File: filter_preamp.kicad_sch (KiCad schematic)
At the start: 24 parts, among them J2 Conn_Coaxial, Q1 2N2222A, Q2 2N2222A

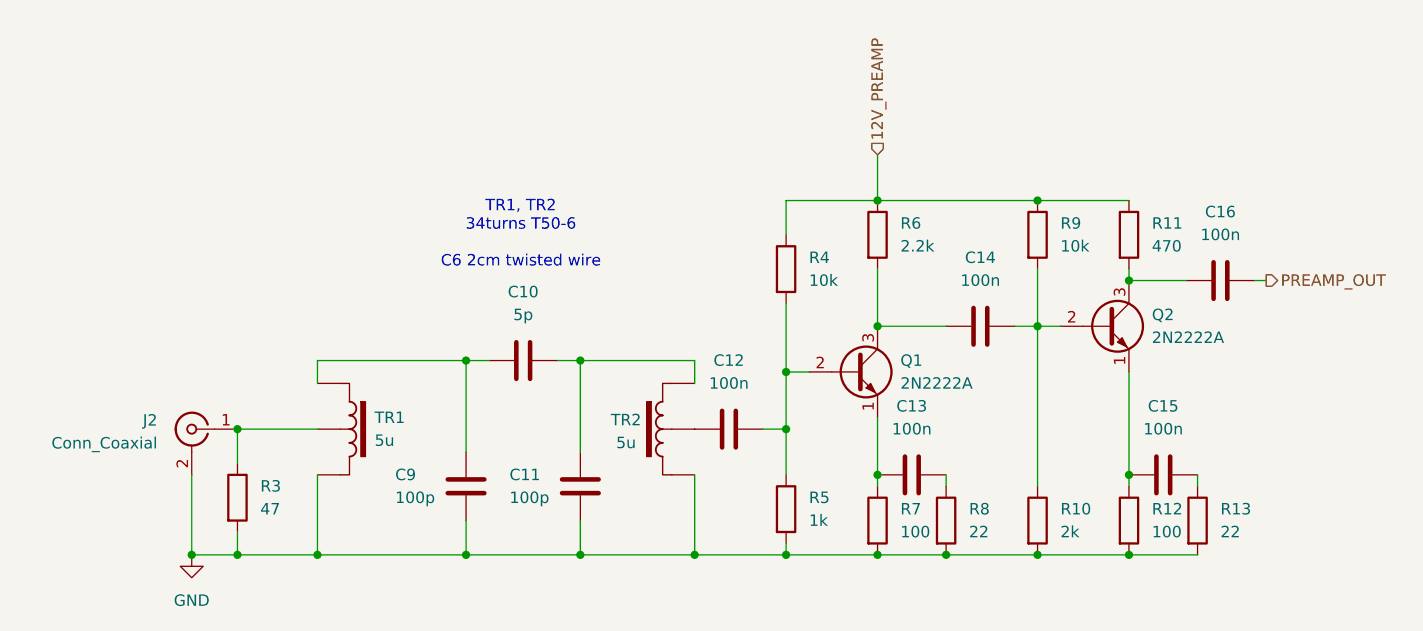
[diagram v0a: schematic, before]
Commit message: Update transformer comment
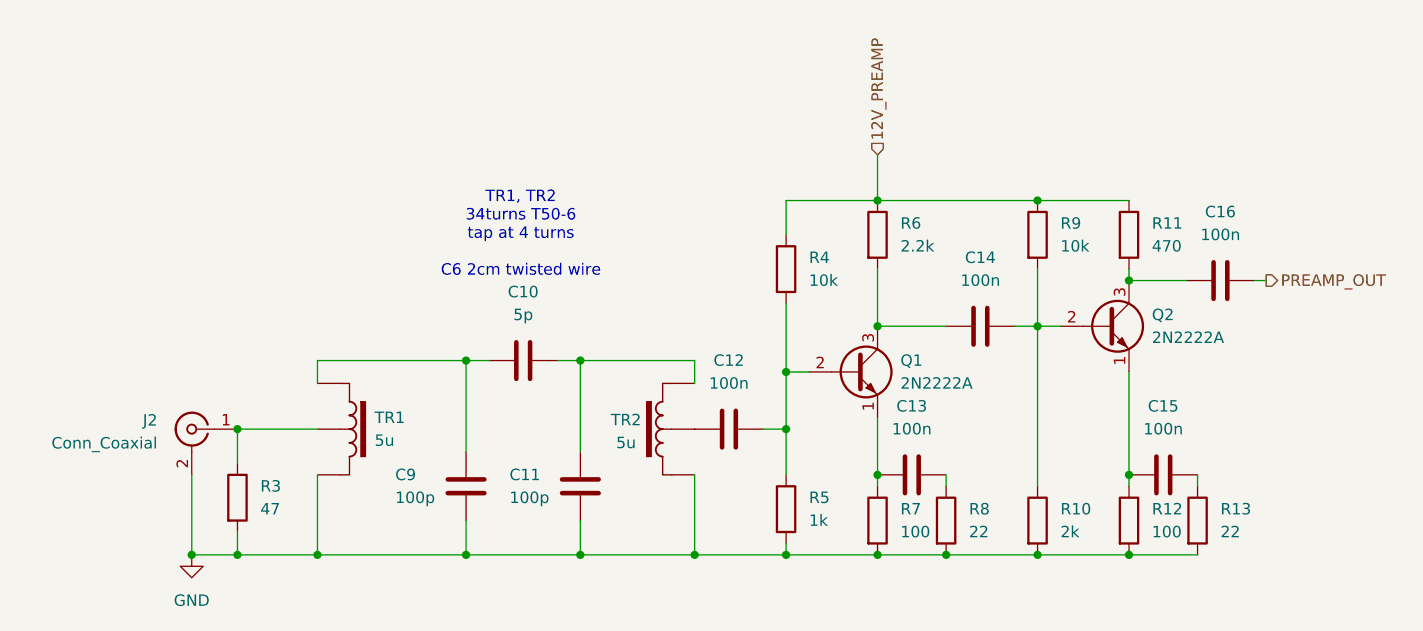
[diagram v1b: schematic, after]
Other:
- note added: "TR1, TR2 34turns T50-6 tap at 4 turns C6 2cm twisted wire"
- note removed: "TR1, TR2 34turns T50-6 C6 2cm twisted wire"
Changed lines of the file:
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@@
 	(generator_version "9.0")
 	(paper "A4")
-	(text "TR1, TR2\n34turns T50-6\n\nC6 2cm twisted wire"
+	(text "TR1, TR2\n34turns T50-6\ntap at 4 turns\n\nC6 2cm twisted wire"
 		(exclude_from_sim no)
 		(at 82.296 48.26 0)
